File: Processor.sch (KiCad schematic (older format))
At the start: 36 parts, among them IC1 74574N, IC10 74244N, IC11 74244N, IC12 74251N, IC13 74244N, IC14 74244N, IC15 74244N, IC16 74AC163N, IC17 74260N, IC18 7486N, IC19 74133N, IC2 74574N, IC20 74280N, IC21 2764, IC22 2764, IC23 2764, IC3 74257N, IC30 7432N, IC32 74245N, IC33 74AC161N, IC34 74AC161N, IC35 74AC161N, IC36 74AC161N, IC37 74244N, IC38 74244N, IC39 74244N, IC4 74257N, IC40 74244N, IC41 74574N, IC42 74244N, IC43 74373N, IC5 74381N, IC6 74381N, IC7 74574N, IC8 74182N, IC9 7486N

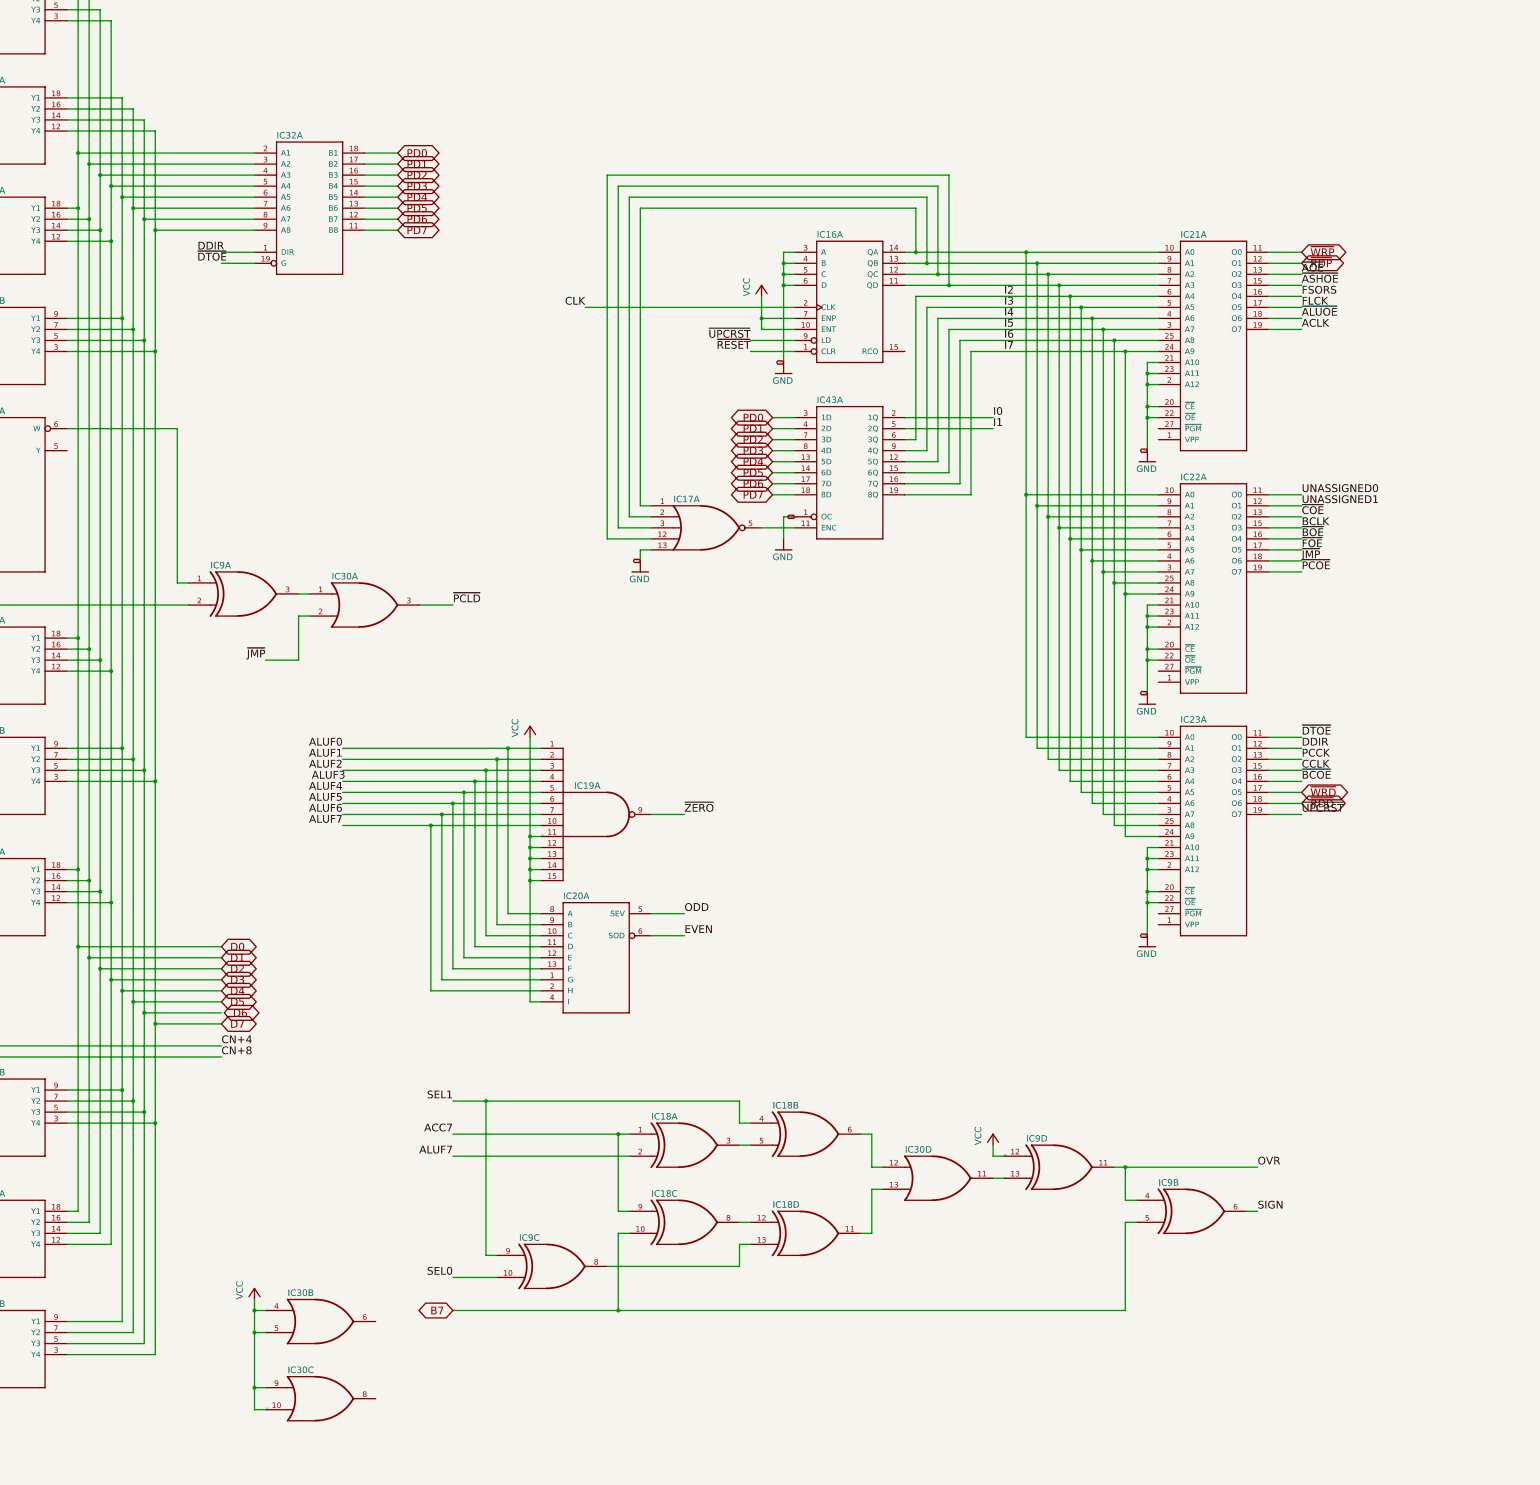
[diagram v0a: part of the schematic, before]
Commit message: Register microcode outputs
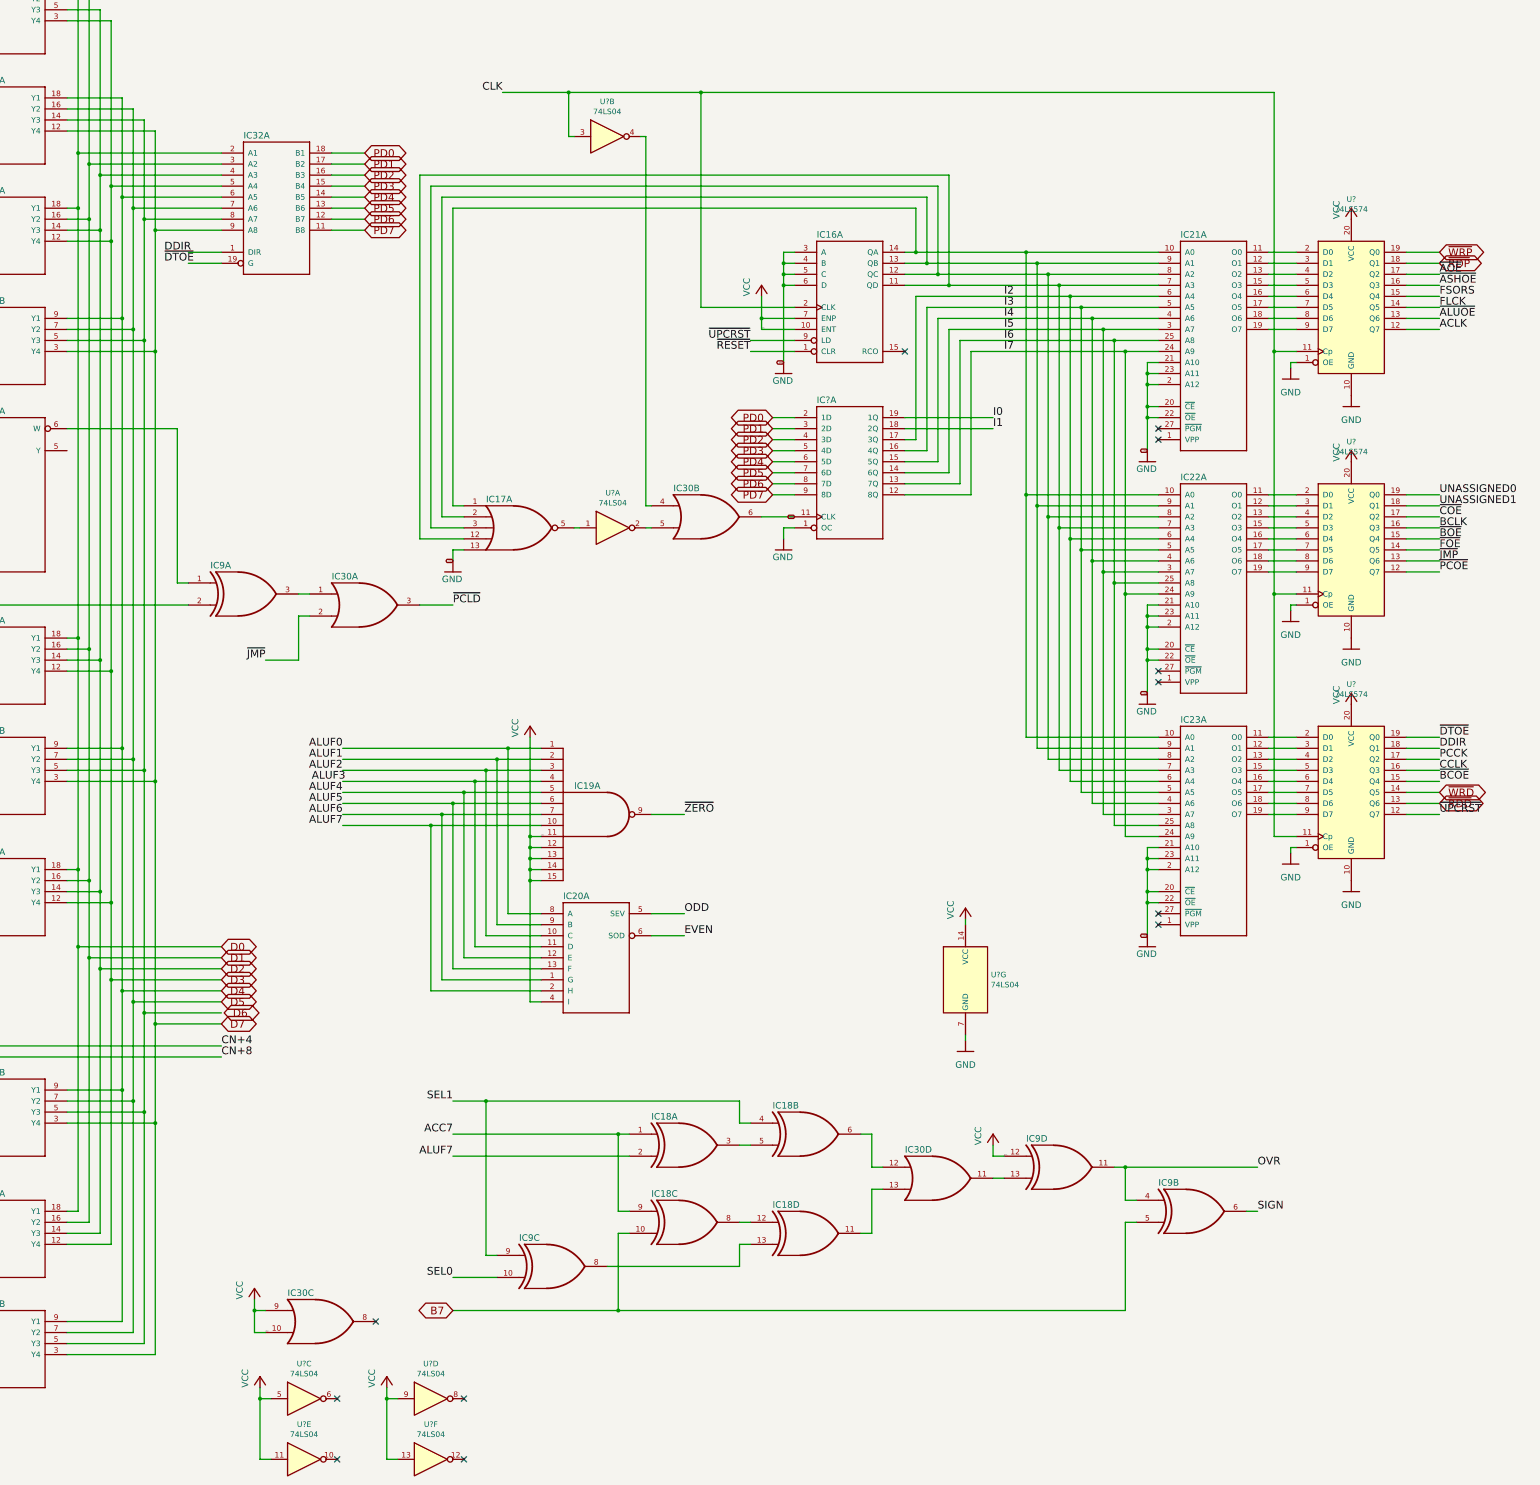
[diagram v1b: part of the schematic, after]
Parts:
- removed IC43: 74373N, MicroComp v1.1:DIL20, symbol MicroComp_v1.1-eagle-import:74373N
- added IC?: 74574N, MicroComp v1.1:DIL20, symbol MicroComp_v1.1-eagle-import:74574N
- added U? (x3): 74LS574, symbol 74xx:74LS574
- added U? (x7): 74LS04, symbol 74xx:74LS04
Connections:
- net ACLK: now also U?.12 (Q7); no longer IC21.19 (O7)
- net BCLK: now also U?.16 (Q3); no longer IC22.15 (O3)
- net CCLK: now also U?.16 (Q3); no longer IC23.15 (O3)
- net CLK: now also U?.11 (Cp), U?.11 (Cp), U?.11 (Cp), U?.3
- net DDIR: now also U?.18 (Q1); no longer IC23.12 (O1)
- net FLCK: now also U?.14 (Q5); no longer IC21.17 (O5)
- net FSORS: now also U?.15 (Q4); no longer IC21.16 (O4)
- net GND: now also IC30.6 (O), IC?.11 (CLK)
- net I0: now also IC?.19 (1Q)
- net I1: now also IC?.18 (2Q)
- net I2: now also IC?.17 (3Q)
- net I3: now also IC?.16 (4Q)
- net I4: now also IC?.15 (5Q)
- net I5: now also IC?.14 (6Q)
- net I6: now also IC?.13 (7Q)
- net I7: now also IC?.12 (8Q)
- net PCCK: now also U?.17 (Q2); no longer IC23.13 (O2)
- net PD0: now also IC?.2 (1D)
- net PD1: now also IC?.3 (2D)
- net PD2: now also IC?.4 (3D)
- net PD3: now also IC?.5 (4D)
- net PD4: now also IC?.6 (5D)
- net PD5: now also IC?.7 (6D)
- net PD6: now also IC?.8 (7D)
- net PD7: now also IC?.9 (8D)
- net UNASSIGNED0: now also U?.19 (Q0); no longer IC22.11 (O0)
- net UNASSIGNED1: now also U?.18 (Q1); no longer IC22.12 (O1)
- net VCC: no longer IC30.4 (I0), IC30.5 (I1)
- net ~ALUOE: now also U?.13 (Q6); no longer IC21.18 (O6)
- net ~AOE: now also U?.17 (Q2); no longer IC21.13 (O2)
- net ~ASHOE: now also U?.16 (Q3); no longer IC21.15 (O3)
- net ~BCOE: now also U?.15 (Q4); no longer IC23.16 (O4)
- net ~BOE: now also U?.15 (Q4); no longer IC22.16 (O4)
- net ~COE: now also U?.17 (Q2); no longer IC22.13 (O2)
- net ~DTOE: now also U?.19 (Q0); no longer IC23.11 (O0)
- net ~FOE: now also U?.14 (Q5); no longer IC22.17 (O5)
- net ~JMP: now also U?.13 (Q6); no longer IC22.18 (O6)
- net ~PCOE: now also U?.12 (Q7); no longer IC22.19 (O7)
- net ~RDD: now also U?.13 (Q6); no longer IC23.18 (O6)
- net ~RDP: now also U?.18 (Q1); no longer IC21.12 (O1)
- net ~UPCRST: now also U?.12 (Q7); no longer IC23.19 (O7)
- net ~WRD: now also U?.14 (Q5); no longer IC23.17 (O5)
- net ~WRP: now also U?.19 (Q0); no longer IC21.11 (O0)
- net at IC17.5 (O): now also U?.1
- new net: IC21.11 (O0), U?.2 (D0)
- new net: IC21.12 (O1), U?.3 (D1)
- new net: IC21.13 (O2), U?.4 (D2)
- new net: IC21.15 (O3), U?.5 (D3)
- new net: IC21.16 (O4), U?.6 (D4)
- new net: IC21.17 (O5), U?.7 (D5)
- new net: IC21.18 (O6), U?.8 (D6)
- new net: IC21.19 (O7), U?.9 (D7)
- new net: IC22.11 (O0), U?.2 (D0)
- new net: IC22.12 (O1), U?.3 (D1)
- new net: IC22.13 (O2), U?.4 (D2)
- new net: IC22.15 (O3), U?.5 (D3)
- new net: IC22.16 (O4), U?.6 (D4)
- new net: IC22.17 (O5), U?.7 (D5)
- new net: IC22.18 (O6), U?.8 (D6)
- new net: IC22.19 (O7), U?.9 (D7)
- new net: IC23.11 (O0), U?.2 (D0)
- new net: IC23.12 (O1), U?.3 (D1)
- new net: IC23.13 (O2), U?.4 (D2)
- new net: IC23.15 (O3), U?.5 (D3)
- new net: IC23.16 (O4), U?.6 (D4)
- new net: IC23.17 (O5), U?.7 (D5)
- new net: IC23.18 (O6), U?.8 (D6)
- new net: IC23.19 (O7), U?.9 (D7)
- new net: IC30.5 (I1), U?.2
- new net: IC30.4 (I0), U?.4
- new net: U?.11, U?.5
- new net: U?.13, U?.9
- no-connect marks 0 -> 12
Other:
- moved on the sheet: IC17A, IC30B, IC30C, IC32A
